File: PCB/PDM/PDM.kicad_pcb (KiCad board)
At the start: 2 copper layers, 260 parts, among them IC1 STM32L496ZGT6, IC12 LM5050MK-1_NOPB, IC13 LM5050MK-1_NOPB, IC14 TLE9104SHXUMA1, IC2 AT25SF128A-SHB-T, IC4 TS5A21366DCUR, IC5 TMP126NDCKR, IC6 TMP126NDCKR, IC7 BTS722204ESAXUMA1, IC8 BTS722204ESAXUMA1, Q1 MMBT3904, Q10 STL225N6F7AG, Q11 STL225N6F7AG, Q2 IAUA250N04S6N007AUMA1, Q3 IAUA250N04S6N007AUMA1, Q4 STL135N8F7AG, Q5 STL135N8F7AG, Q6 STL135N8F7AG, Q7 STL135N8F7AG, Q8 STL135N8F7AG, Q9 STL135N8F7AG, U1 VNF1048FTR, U10 VNF1048FTR, U2 MCP2561-E-SN, U3 MCP2561-E-SN, U4 VNF1048FTR, U5 VNF1048FTR, U6 VNF1048FTR, U7 VNF1048FTR, U8 VNF1048FTR, U9 VNF1048FTR, Y1 48Mhz, Y2 32KHz

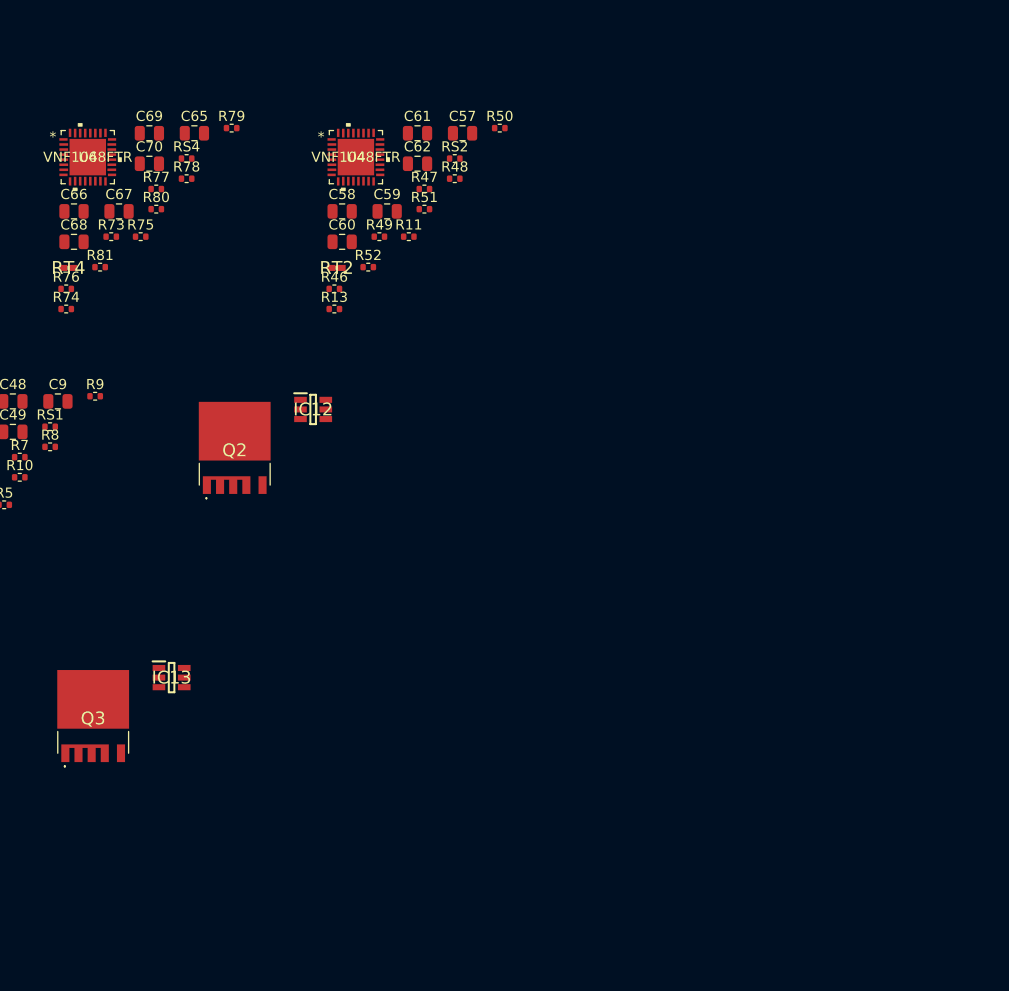
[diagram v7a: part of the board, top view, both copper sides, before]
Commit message: Added fuse on each output of hs section - change footprint later!
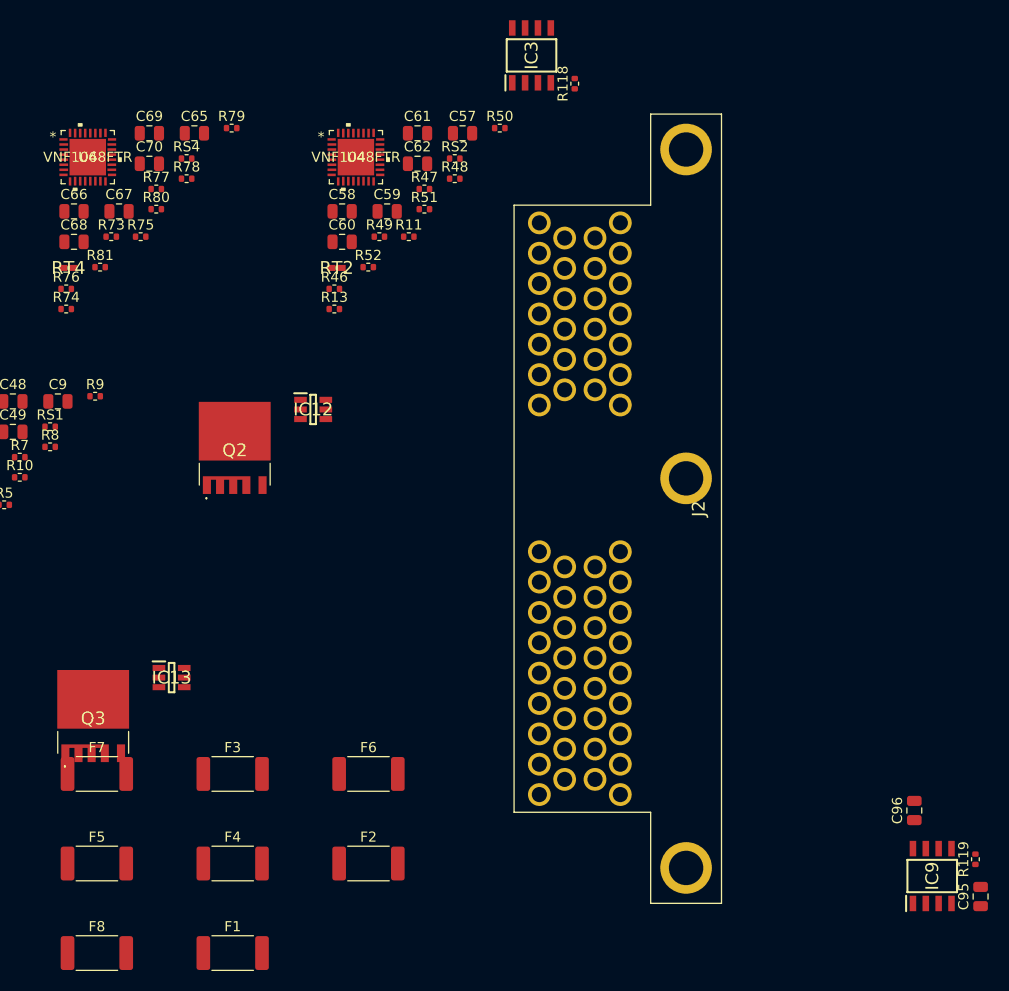
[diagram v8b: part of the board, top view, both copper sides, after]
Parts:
- added C95: 100nF, Capacitor_SMD:C_0805_2012Metric, F.Cu at (279.4, 148.3)
- added C96: 100nF, Capacitor_SMD:C_0805_2012Metric, F.Cu at (272.9, 139.8)
- added F1: 40A, Fuse:Fuse_2512_6332Metric, F.Cu at (205.5, 153.9)
- added F2: 40A, Fuse:Fuse_2512_6332Metric, F.Cu at (218.9, 145.1)
- added F3: 40A, Fuse:Fuse_2512_6332Metric, F.Cu at (205.5, 136.2)
- added F4: 40A, Fuse:Fuse_2512_6332Metric, F.Cu at (205.5, 145.1)
- added F5: 40A, Fuse:Fuse_2512_6332Metric, F.Cu at (192.1, 145.1)
- added F6: 40A, Fuse:Fuse_2512_6332Metric, F.Cu at (218.9, 136.2)
- added F7: 40A, Fuse:Fuse_2512_6332Metric, F.Cu at (192.1, 136.2)
- added F8: 40A, Fuse:Fuse_2512_6332Metric, F.Cu at (192.1, 153.9)
- added IC3: SN65HVD230QDG4Q1, PDM_Additional:SOIC127P600X175-8N, F.Cu at (235.0, 65.2)
- added IC9: SN65HVD230QDG4Q1, PDM_Additional:SOIC127P600X175-8N, F.Cu at (274.6, 146.3)
- added J2: 6473427-1, PDM_Additional:64734271, F.Cu at (235.8, 138.3)
- added R118: 0, Resistor_SMD:R_0402_1005Metric, F.Cu at (239.3, 68.0)
- added R119: 0, Resistor_SMD:R_0402_1005Metric, F.Cu at (278.9, 144.7)
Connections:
- net /HIGH SIDE1/CSN_SECA1 renamed /HIGH SIDE1/CSN1
- net /HIGH SIDE1/CSN_SECA2 renamed /HIGH SIDE1/CSN2
- net /HIGH SIDE1/CSN_SECA3 renamed /HIGH SIDE1/CSN3
- net /HIGH SIDE1/CSN_SECA4 renamed /HIGH SIDE1/CSN4
- net /HIGH SIDE1/CSN_SECA5 renamed /HIGH SIDE1/CSN5
- net /HIGH SIDE1/CSN_SECA6 renamed /HIGH SIDE1/CSN6
- net /HIGH SIDE1/CSN_SECA7 renamed /HIGH SIDE1/CSN7
- net /HIGH SIDE1/CSN_SECA8 renamed /HIGH SIDE1/CSN8
- net /MCU/NCS_SECA1 renamed /MCU/CSN_SECA1
- net /MCU/NCS_SECA2 renamed /MCU/CSN_SECA2
- net /MCU/NCS_SECA3 renamed /MCU/CSN_SECA3
- net /MCU/NCS_SECA4 renamed /MCU/CSN_SECA4
- net /MCU/NCS_SECA5 renamed /MCU/CSN_SECA5
- net /MCU/NCS_SECA6 renamed /MCU/CSN_SECA6
- C50 pad 1: VDD -> GND
- C57 pad 1: VDD -> GND
- C65 pad 1: VDD -> GND
- C71 pad 1: VDD -> GND
- C77 pad 1: VDD -> GND
- C83 pad 1: VDD -> GND
- C89 pad 1: VDD -> GND
- C9 pad 1: VDD -> GND
- IC1 pad 135: unconnected-(IC1-Pad135) -> /MCU/PWM_OUT2
- IC1 pad 139: /MCU/CAN1_RX -> CAN1_RX
- IC1 pad 140: /MCU/CAN1_TX -> CAN1_TX
- IC1 pad 73: /MCU/CAN2_RX -> CAN2_RX
- IC1 pad 74: /MCU/CAN2_TX -> CAN2_TX
- R72 pad 1: /USER PERIPHERAL/BUZZ_IN -> /MCU/PWM_OUT2
